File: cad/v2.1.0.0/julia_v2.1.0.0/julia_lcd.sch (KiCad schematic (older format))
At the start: 15 parts, among them J4 Molex 0541044031, J5 Molex 0522710679, U7 FAN5333BSX

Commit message: Swap FAN5333BSX backlight driver for TPS61165
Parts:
- removed D6: MM3Z18VT1G, symbol Device:D_Zener
- removed R9: 10k, symbol Device:R
- removed U7: FAN5333BSX, Package_TO_SOT_SMD:SOT-23-5, symbol ik:FAN5333BSX
- added U7: TPS61165_WSON, ik:TPS61165_WSON-6, symbol ik:TPS61165_WSON
- C43: value 10uF -> 4.7uF
- C44: value 1uF,60V -> 220nF
- C45: value 0.1uF -> 1uF
- R10: value 5.6 -> 3.3
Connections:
- wire segments 101 -> 97
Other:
- note removed: "TODO: analog dim"
- moved on the sheet: C43, R10
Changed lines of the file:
@@
-$EndComp
-$Comp
-L ik:FAN5333BSX U7
-U 1 1 60724BAB
-P 2500 2150
-F 0 "U7" H 2500 2515 50  0000 C CNN
-F 1 "FAN5333BSX" H 2500 2424 50  0000 C CNN
-F 2 "Package_TO_SOT_SMD:SOT-23-5" H 2500 1850 50  0001 C CNN
-F 3 "" H 2500 2150 50  0001 C CNN
-	1    2500 2150
-	1    0    0    -1
 $EndComp
 $Comp
 L power:+5V #PWR0137
 U 1 1 60725F4B
-P 1700 1450
-F 0 "#PWR0137" H 1700 1300 50  0001 C CNN
-F 1 "+5V" H 1715 1623 50  0000 C CNN
-F 2 "" H 1700 1450 50  0001 C CNN
-F 3 "" H 1700 1450 50  0001 C CNN
-	1    1700 1450
-	1    0    0    -1
-$EndComp
-$Comp
-L power:GND #PWR0138
-U 1 1 60726411
-P 1350 3100
-F 0 "#PWR0138" H 1350 2850 50  0001 C CNN
-F 1 "GND" H 1355 2927 50  0000 C CNN
-F 2 "" H 1350 3100 50  0001 C CNN
-F 3 "" H 1350 3100 50  0001 C CNN
-	1    1350 3100
+P 1100 1550
+F 0 "#PWR0137" H 1100 1400 50  0001 C CNN
+F 1 "+5V" H 1115 1723 50  0000 C CNN
+F 2 "" H 1100 1550 50  0001 C CNN
+F 3 "" H 1100 1550 50  0001 C CNN
+	1    1100 1550
 	1    0    0    -1
 $EndComp
@@
 L Device:C C43
 U 1 1 60726867
-P 1700 2550
-F 0 "C43" H 1815 2596 50  0000 L CNN
-F 1 "10uF" H 1815 2505 50  0000 L CNN
-F 2 "" H 1738 2400 50  0001 C CNN
-F 3 "~" H 1700 2550 50  0001 C CNN
-	1    1700 2550
+P 1150 2050
+F 0 "C43" H 1265 2096 50  0000 L CNN
+F 1 "4.7uF" H 1265 2005 50  0000 L CNN
+F 2 "" H 1188 1900 50  0001 C CNN
+F 3 "~" H 1150 2050 50  0001 C CNN
+	1    1150 2050
 	1    0    0    -1
 $EndComp
@@
 $EndComp
 $Comp
-L Device:D_Zener D6
-U 1 1 6072797E
-P 4300 1850
-F 0 "D6" V 4254 1930 50  0000 L CNN
-F 1 "MM3Z18VT1G" V 4345 1930 50  0000 L CNN
-F 2 "" H 4300 1850 50  0001 C CNN
-F 3 "~" H 4300 1850 50  0001 C CNN
-	1    4300 1850
-	0    1    1    0
-$EndComp
-$Comp
-L Device:C C45
-U 1 1 60728167
-P 4300 2500
-F 0 "C45" H 4415 2546 50  0000 L CNN
-F 1 "0.1uF" H 4415 2455 50  0000 L CNN
-F 2 "" H 4338 2350 50  0001 C CNN
-F 3 "~" H 4300 2500 50  0001 C CNN
-	1    4300 2500
-	1    0    0    -1
-$EndComp
-$Comp
 L Device:R R10
 U 1 1 60728526
-P 3400 2500
-F 0 "R10" H 3470 2546 50  0000 L CNN
-F 1 "5.6" H 3470 2455 50  0000 L CNN
-F 2 "" V 3330 2500 50  0001 C CNN
-F 3 "~" H 3400 2500 50  0001 C CNN
-	1    3400 2500
-	1    0    0    -1
-$EndComp
-Text HLabel 1150 2250 0    50   Input ~ 0
+P 3250 2550
+F 0 "R10" H 3320 2596 50  0000 L CNN
+F 1 "3.3" H 3320 2505 50  0000 L CNN
+F 2 "" V 3180 2550 50  0001 C CNN
+F 3 "~" H 3250 2550 50  0001 C CNN
+	1    3250 2550
+	1    0    0    -1
+$EndComp
+Text HLabel 1600 2250 0    50   Input ~ 0
 LIGHT
-$Comp
-L Device:R R9
-U 1 1 6072D898
-P 1350 2550
-F 0 "R9" H 1420 2596 50  0000 L CNN
-F 1 "10k" H 1420 2505 50  0000 L CNN
-F 2 "" V 1280 2550 50  0001 C CNN
-F 3 "~" H 1350 2550 50  0001 C CNN
-	1    1350 2550
-	1    0    0    -1
-$EndComp
-Wire Wire Line
-	1150 2250 1350 2250
-Wire Wire Line
-	1350 2250 1350 2400
-Connection ~ 1350 2250
-Wire Wire Line
-	1350 2250 2100 2250
-Wire Wire Line
-	1700 2050 1950 2050
-Connection ~ 1700 2050
-Wire Wire Line
-	1700 2050 1700 2400
-Wire Wire Line
-	1700 1450 1700 2050
-Wire Wire Line
-	1950 2050 1950 1650
-Wire Wire Line
-	1950 1650 2350 1650
-Connection ~ 1950 2050
-Wire Wire Line
-	1950 2050 2100 2050
-Wire Wire Line
-	2650 1650 3000 1650
-Wire Wire Line
-	2900 2050 3000 2050
-Wire Wire Line
-	3000 2050 3000 1650
-Connection ~ 3000 1650
-Wire Wire Line
-	3000 1650 3200 1650
-Wire Wire Line
-	4300 1650 4300 1700
-Connection ~ 4300 1650
 Text Label 4600 1650 2    50   ~ 0
 LED+
-Wire Wire Line
-	4300 2000 4300 2300
-Text Label 4600 2300 2    50   ~ 0
+Text Label 4600 2450 2    50   ~ 0
 LED-
-Wire Wire Line
-	4300 2300 4300 2350
-Connection ~ 4300 2300
-Wire Wire Line
-	4300 2650 4300 2950
-Wire Wire Line
-	1350 2700 1350 3100
-Wire Wire Line
-	1700 2950 2800 2950
-Wire Wire Line
-	1700 2700 1700 2950
-$Comp
-L power:GND #PWR0139
-U 1 1 60734B25
-P 2800 3100
-F 0 "#PWR0139" H 2800 2850 50  0001 C CNN
-F 1 "GND" H 2805 2927 50  0000 C CNN
-F 2 "" H 2800 3100 50  0001 C CNN
-F 3 "" H 2800 3100 50  0001 C CNN
-	1    2800 3100
-	1    0    0    -1
-$EndComp
-Wire Wire Line
-	2800 3100 2800 2950
-Connection ~ 2800 2950
-Wire Wire Line
-	2800 2950 2900 2950
-Wire Wire Line
-	2900 2250 2900 2950
-Connection ~ 2900 2950
-Wire Wire Line
-	2900 2950 3400 2950
-Wire Wire Line
-	3400 2650 3400 2950
-Connection ~ 3400 2950
-Wire Wire Line
-	3800 1650 4300 1650
-Wire Wire Line
-	3500 1650 3800 1650
-Connection ~ 3800 1650
-Wire Wire Line
-	3800 1650 3800 1700
-$Comp
-L Device:C C44
-U 1 1 60727DE9
-P 3800 1850
-F 0 "C44" H 3915 1896 50  0000 L CNN
-F 1 "1uF,60V" H 3915 1805 50  0000 L CNN
-F 2 "" H 3838 1700 50  0001 C CNN
-F 3 "~" H 3800 1850 50  0001 C CNN
-	1    3800 1850
-	1    0    0    -1
-$EndComp
-Wire Wire Line
-	3400 2950 4300 2950
 $Comp
 L power:GND #PWR0140
 U 1 1 6073FDBF
-P 3800 2050
-F 0 "#PWR0140" H 3800 1800 50  0001 C CNN
-F 1 "GND" H 3805 1877 50  0000 C CNN
-F 2 "" H 3800 2050 50  0001 C CNN
-F 3 "" H 3800 2050 50  0001 C CNN
-	1    3800 2050
-	1    0    0    -1
-$EndComp
-Wire Wire Line
-	2900 2150 3200 2150
-Wire Wire Line
-	3200 2150 3200 2300
-Wire Wire Line
-	3200 2300 3400 2300
-Wire Wire Line
-	3400 2350 3400 2300
-Connection ~ 3400 2300
-Wire Wire Line
-	3400 2300 4300 2300
-Wire Wire Line
-	3800 2000 3800 2050
+P 3700 2200
+F 0 "#PWR0140" H 3700 1950 50  0001 C CNN
+F 1 "GND" H 3705 2027 50  0000 C CNN
+F 2 "" H 3700 2200 50  0001 C CNN
+F 3 "" H 3700 2200 50  0001 C CNN
+	1    3700 2200
+	1    0    0    -1
+$EndComp
 Text Label 8400 1850 1    50   ~ 0
 RGB[0..23]
@@
 Text Label 8550 3550 0    50   ~ 0
 RGB23
-Text Notes 750  2200 0    50   ~ 0
-TODO: analog dim
 $Comp
 L power:+3V3 #PWR0141
@@
 	5950 950  8850 950
 Wire Wire Line
-	4300 1650 5950 1650
-Wire Wire Line
-	6100 2300 6100 850
+	6100 2450 6100 850
 Wire Wire Line
 	6100 850  8850 850
-Wire Wire Line
-	4300 2300 6100 2300
 $Comp
 L power:GND #PWR0143
@@
 	8050 5000 7750 5000
 Connection ~ 7750 5000
+$Comp
+L ik:TPS61165_WSON U7
+U 1 1 5FF5A409
+P 2500 2250
+F 0 "U7" H 2500 2717 50  0000 C CNN
+F 1 "TPS61165_WSON" H 2500 2626 50  0000 C CNN
+F 2 "ik:TPS61165_WSON-6" H 2450 1350 50  0001 C CNN
+F 3 "" H 2500 2250 50  0001 C CNN
+	1    2500 2250
+	1    0    0    -1
+$EndComp
+Wire Wire Line
+	2100 2050 1800 2050
+Wire Wire Line
+	1800 2050 1800 1650
+Wire Wire Line
+	1800 1650 2350 1650
+Wire Wire Line
+	2650 1650 3050 1650
+Wire Wire Line
+	2900 2050 3050 2050
+Wire Wire Line
+	3050 2050 3050 1650
+Connection ~ 3050 1650
+Wire Wire Line
+	3050 1650 3200 1650
+$Comp
+L Device:C C44
+U 1 1 5FF614BE
+P 1800 2800
+F 0 "C44" H 1915 2846 50  0000 L CNN
+F 1 "220nF" H 1915 2755 50  0000 L CNN
+F 2 "" H 1838 2650 50  0001 C CNN
+F 3 "~" H 1800 2800 50  0001 C CNN
+	1    1800 2800
+	1    0    0    -1
+$EndComp
+$Comp
+L Device:C C45
+U 1 1 5FF618DE
+P 3700 1900
+F 0 "C45" H 3815 1946 50  0000 L CNN
+F 1 "1uF" H 3815 1855 50  0000 L CNN
+F 2 "" H 3738 1750 50  0001 C CNN
+F 3 "~" H 3700 1900 50  0001 C CNN
+	1    3700 1900
+	1    0    0    -1
+$EndComp
+Wire Wire Line
+	1100 1550 1100 1650
+Wire Wire Line
+	1100 1650 1150 1650
+Connection ~ 1800 1650
+Wire Wire Line
+	3700 2050 3700 2200
+Wire Wire Line
+	3500 1650 3700 1650
+Wire Wire Line
+	3500 2450 3500 2250
+Wire Wire Line
+	3500 2250 3250 2250
+Wire Wire Line
+	3250 2400 3250 2250
+Wire Wire Line
+	3000 2450 2900 2450
+Connection ~ 3250 2250
+Wire Wire Line
+	3250 2250 2900 2250
+Wire Wire Line
+	3500 2450 6100 2450
+Wire Wire Line
+	3700 1750 3700 1650
+Connection ~ 3700 1650
+Wire Wire Line
+	3700 1650 5950 1650
+Wire Wire Line
+	1150 1900 1150 1650
+Connection ~ 1150 1650
+Wire Wire Line
+	1150 1650 1800 1650
+Wire Wire Line
+	1800 2650 1800 2450
+Wire Wire Line
+	1800 2450 2100 2450
+$Comp
+L power:GND #PWR0138
+U 1 1 5FF97960
+P 2400 3150
+F 0 "#PWR0138" H 2400 2900 50  0001 C CNN
+F 1 "GND" H 2405 2977 50  0000 C CNN
+F 2 "" H 2400 3150 50  0001 C CNN
+F 3 "" H 2400 3150 50  0001 C CNN
+	1    2400 3150
+	1    0    0    -1
+$EndComp
+Wire Wire Line
+	1150 3100 1800 3100
+Wire Wire Line
+	3250 3100 3250 2700
+Wire Wire Line
+	1150 2200 1150 3100
+Wire Wire Line
+	3000 2450 3000 3100
+Connection ~ 3000 3100
+Wire Wire Line
+	3000 3100 3250 3100
+Wire Wire Line
+	1800 2950 1800 3100
+Connection ~ 1800 3100
+Wire Wire Line
+	1800 3100 2400 3100
+Wire Wire Line
+	1600 2250 2100 2250
+Wire Wire Line
+	2400 3150 2400 3100
 Wire Bus Line
 	8400 1100 8400 3550
+Connection ~ 2400 3100
+Wire Wire Line
+	2400 3100 3000 3100
 $EndSCHEMATC

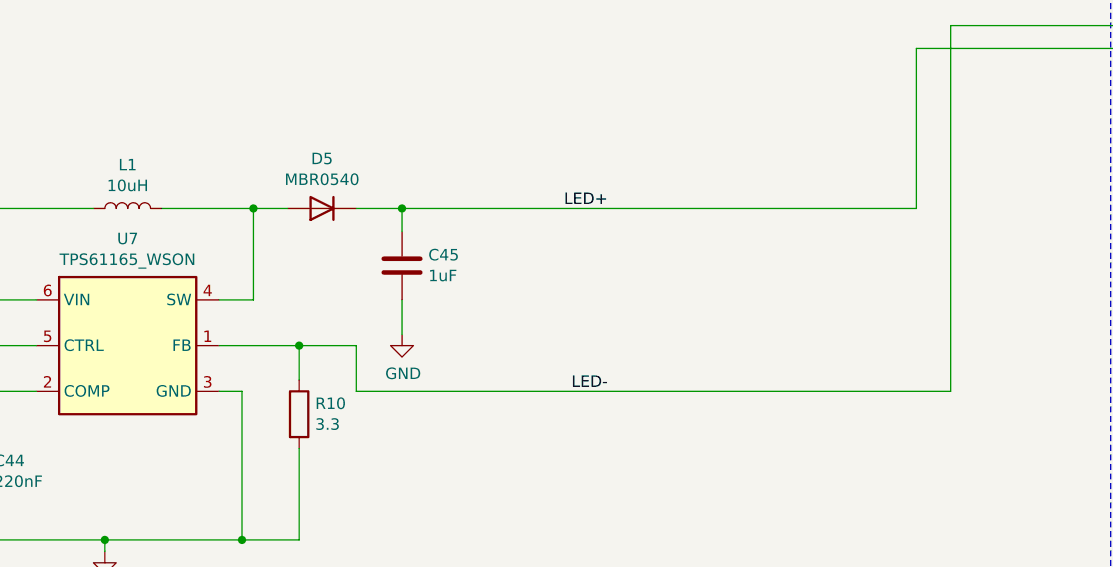
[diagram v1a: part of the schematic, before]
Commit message: v2.1.0.0: changed connector, ERC, annotation/footprint assignment
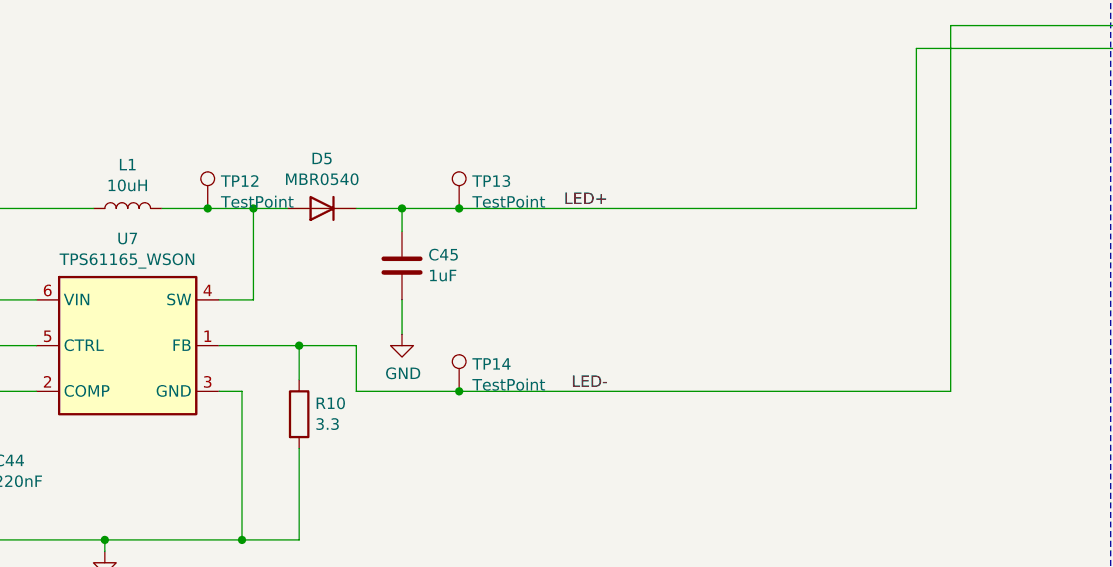
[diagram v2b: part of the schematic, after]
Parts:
- added TP12, TP13, TP14: TestPoint, TestPoint:TestPoint_THTPad_D1.0mm_Drill0.5mm, symbol Connector:TestPoint
- C43, C44, C45: footprint (none) -> Capacitor_SMD:C_0603_1608Metric
- D5: footprint (none) -> Diode_SMD:D_SOD-123
- J4: footprint (none) -> ik:Molex_54104-4031_1x40-P0.5mm_Horizontal
- J5: footprint (none) -> ik:Molex_52271-0679_1x06-1MP_P1.00mm_Horizontal
- L1: footprint (none) -> ik:Murata_D53LC_A915AY-100M
- R10: footprint (none) -> Resistor_SMD:R_0805_2012Metric
- R11, R12, R13, R14: footprint (none) -> Resistor_SMD:R_0402_1005Metric
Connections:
- net LED+: now also TP13.1
- net LED-: now also TP14.1
- net at D5.2 (A), L1.2, U7.4 (SW): now also TP12.1
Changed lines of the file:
@@
 F 0 "J4" H 9078 2726 50  0000 L CNN
 F 1 "Molex 0541044031" H 9078 2635 50  0000 L CNN
-F 2 "" H 9050 2750 50  0001 C CNN
+F 2 "ik:Molex_54104-4031_1x40-P0.5mm_Horizontal" H 9050 2750 50  0001 C CNN
 F 3 "~" H 9050 2750 50  0001 C CNN
 	1    9050 2750
@@
 F 0 "J5" H 9078 5576 50  0000 L CNN
 F 1 "Molex 0522710679" H 9078 5485 50  0000 L CNN
-F 2 "" H 9050 5600 50  0001 C CNN
+F 2 "ik:Molex_52271-0679_1x06-1MP_P1.00mm_Horizontal" H 9050 5600 50  0001 C CNN
 F 3 "~" H 9050 5600 50  0001 C CNN
 	1    9050 5600
@@
 F 0 "C43" H 1265 2096 50  0000 L CNN
 F 1 "4.7uF" H 1265 2005 50  0000 L CNN
-F 2 "" H 1188 1900 50  0001 C CNN
+F 2 "Capacitor_SMD:C_0603_1608Metric" H 1188 1900 50  0001 C CNN
 F 3 "~" H 1150 2050 50  0001 C CNN
 	1    1150 2050
@@
 F 0 "L1" V 2690 1650 50  0000 C CNN
 F 1 "10uH" V 2599 1650 50  0000 C CNN
-F 2 "" H 2500 1650 50  0001 C CNN
+F 2 "ik:Murata_D53LC_A915AY-100M" H 2500 1650 50  0001 C CNN
 F 3 "~" H 2500 1650 50  0001 C CNN
 	1    2500 1650
@@
 F 0 "D5" H 3350 1433 50  0000 C CNN
 F 1 "MBR0540" H 3350 1524 50  0000 C CNN
-F 2 "" H 3350 1650 50  0001 C CNN
+F 2 "Diode_SMD:D_SOD-123" H 3350 1650 50  0001 C CNN
 F 3 "~" H 3350 1650 50  0001 C CNN
 	1    3350 1650
@@
 F 0 "R10" H 3320 2596 50  0000 L CNN
 F 1 "3.3" H 3320 2505 50  0000 L CNN
-F 2 "" V 3180 2550 50  0001 C CNN
+F 2 "Resistor_SMD:R_0805_2012Metric" V 3180 2550 50  0001 C CNN
 F 3 "~" H 3250 2550 50  0001 C CNN
 	1    3250 2550
@@
 F 0 "R14" H 8120 5296 50  0000 L CNN
 F 1 "10k" H 8120 5205 50  0000 L CNN
-F 2 "" V 7980 5250 50  0001 C CNN
+F 2 "Resistor_SMD:R_0402_1005Metric" V 7980 5250 50  0001 C CNN
 F 3 "~" H 8050 5250 50  0001 C CNN
 	1    8050 5250
@@
 F 0 "R11" H 7520 5296 50  0000 L CNN
 F 1 "10k" H 7520 5205 50  0000 L CNN
-F 2 "" V 7380 5250 50  0001 C CNN
+F 2 "Resistor_SMD:R_0402_1005Metric" V 7380 5250 50  0001 C CNN
 F 3 "~" H 7450 5250 50  0001 C CNN
 	1    7450 5250
@@
 F 0 "R12" H 7820 5296 50  0000 L CNN
 F 1 "10k" H 7820 5205 50  0000 L CNN
-F 2 "" V 7680 5250 50  0001 C CNN
+F 2 "Resistor_SMD:R_0402_1005Metric" V 7680 5250 50  0001 C CNN
 F 3 "~" H 7750 5250 50  0001 C CNN
 	1    7750 5250
@@
 F 0 "R13" H 7920 6046 50  0000 L CNN
 F 1 "10k" H 7920 5955 50  0000 L CNN
-F 2 "" V 7780 6000 50  0001 C CNN
+F 2 "Resistor_SMD:R_0402_1005Metric" V 7780 6000 50  0001 C CNN
 F 3 "~" H 7850 6000 50  0001 C CNN
 	1    7850 6000
@@
 U 1 1 5FF5A409
 P 2500 2250
+AR Path="/5FF5A409" Ref="U7"  Part="1"
+AR Path="/5FEF89EA/5FF5A409" Ref="U7"  Part="1"
 F 0 "U7" H 2500 2717 50  0000 C CNN
 F 1 "TPS61165_WSON" H 2500 2626 50  0000 C CNN
@@
 	1800 1650 2350 1650
 Wire Wire Line
-	2650 1650 3050 1650
+	2650 1650 2850 1650
 Wire Wire Line
 	2900 2050 3050 2050
@@
 F 0 "C44" H 1915 2846 50  0000 L CNN
 F 1 "220nF" H 1915 2755 50  0000 L CNN
-F 2 "" H 1838 2650 50  0001 C CNN
+F 2 "Capacitor_SMD:C_0603_1608Metric" H 1838 2650 50  0001 C CNN
 F 3 "~" H 1800 2800 50  0001 C CNN
 	1    1800 2800
@@
 F 0 "C45" H 3815 1946 50  0000 L CNN
 F 1 "1uF" H 3815 1855 50  0000 L CNN
-F 2 "" H 3738 1750 50  0001 C CNN
+F 2 "Capacitor_SMD:C_0603_1608Metric" H 3738 1750 50  0001 C CNN
 F 3 "~" H 3700 1900 50  0001 C CNN
 	1    3700 1900
@@
 	3250 2250 2900 2250
 Wire Wire Line
-	3500 2450 6100 2450
+	3500 2450 3950 2450
 Wire Wire Line
 	3700 1750 3700 1650
 Connection ~ 3700 1650
 Wire Wire Line
-	3700 1650 5950 1650
+	3700 1650 3950 1650
 Wire Wire Line
 	1150 1900 1150 1650
@@
 Wire Wire Line
 	2400 3150 2400 3100
+Connection ~ 2400 3100
+Wire Wire Line
+	2400 3100 3000 3100
+$Comp
+L Connector:TestPoint TP13
+U 1 1 6001CBAC
+P 3950 1650
+F 0 "TP13" H 4008 1768 50  0000 L CNN
+F 1 "TestPoint" H 4008 1677 50  0000 L CNN
+F 2 "TestPoint:TestPoint_THTPad_D1.0mm_Drill0.5mm" H 4150 1650 50  0001 C CNN
+F 3 "~" H 4150 1650 50  0001 C CNN
+	1    3950 1650
+	1    0    0    -1
+$EndComp
+Connection ~ 3950 1650
+Wire Wire Line
+	3950 1650 5950 1650
+$Comp
+L Connector:TestPoint TP14
+U 1 1 6001D2C8
+P 3950 2450
+F 0 "TP14" H 4008 2568 50  0000 L CNN
+F 1 "TestPoint" H 4008 2477 50  0000 L CNN
+F 2 "TestPoint:TestPoint_THTPad_D1.0mm_Drill0.5mm" H 4150 2450 50  0001 C CNN
+F 3 "~" H 4150 2450 50  0001 C CNN
+	1    3950 2450
+	1    0    0    -1
+$EndComp
+Connection ~ 3950 2450
+Wire Wire Line
+	3950 2450 6100 2450
+$Comp
+L Connector:TestPoint TP12
+U 1 1 6001D676
+P 2850 1650
+F 0 "TP12" H 2908 1768 50  0000 L CNN
+F 1 "TestPoint" H 2908 1677 50  0000 L CNN
+F 2 "TestPoint:TestPoint_THTPad_D1.0mm_Drill0.5mm" H 3050 1650 50  0001 C CNN
+F 3 "~" H 3050 1650 50  0001 C CNN
+	1    2850 1650
+	1    0    0    -1
+$EndComp
+Connection ~ 2850 1650
+Wire Wire Line
+	2850 1650 3050 1650
 Wire Bus Line
 	8400 1100 8400 3550
-Connection ~ 2400 3100
-Wire Wire Line
-	2400 3100 3000 3100
 $EndSCHEMATC
